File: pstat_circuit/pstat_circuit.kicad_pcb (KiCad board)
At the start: 2 copper layers, 124.5 x 53.3 mm, 40 parts, among them P1 LMP91000-2, P2 LMP91000-2, P3 LMP91000-2, P4 LMP91000-2, P5 LMP91000-2, P6 PWR_BUS, P7 PSTAT_CTRL, P8 I2C_BUS, U1 MCP1700-2, U2 CD4051BM96-2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

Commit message: Replace 10K ohm load resistor with 0.1uF capacitor on 2V5 output of MCP1700
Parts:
- removed R6: 10K, Resistors_SMD:R_0805_HandSoldering
- added C16: 0.1uF, Capacitors_SMD:C_0805_HandSoldering, F.Cu at (81.8, 96.0)
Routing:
- net GND: track 131.2 -> 132.2 mm
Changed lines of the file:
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@@
     (links 133)
     (no_connects 1)
-    (area 67.488999 70.282999 193.019 123.773001)
+    (area 67.488999 70.282999 192.099001 123.773001)
     (thickness 1.6)
     (drawings 23)
-    (tracks 777)
+    (tracks 780)
     (zones 0)
     (modules 40)
@@
   )
   (module Resistors_SMD:R_0805_HandSoldering (layer F.Cu)
-    (at 171.958 100.076 90)
-    (descr "Resistor SMD 0805, hand soldering")
-    (tags "resistor 0805")
-    (attr smd)
-    (fp_text reference R6 (at 3.556 0 90) (layer F.SilkS)
-      (effects (font (size 1 1) (thickness 0.15)))
-    )
-    (fp_text value 10K (at 0 0 90) (layer F.Fab)
-      (effects (font (size 1 1) (thickness 0.15)))
-    )
-    (fp_line (start -2.4 -1) (end 2.4 -1) (layer F.CrtYd) (width 0.05))
-    (fp_line (start -2.4 1) (end 2.4 1) (layer F.CrtYd) (width 0.05))
-    (fp_line (start -2.4 -1) (end -2.4 1) (layer F.CrtYd) (width 0.05))
-    (fp_line (start 2.4 -1) (end 2.4 1) (layer F.CrtYd) (width 0.05))
-    (fp_line (start 0.6 0.875) (end -0.6 0.875) (layer F.SilkS) (width 0.15))
-    (fp_line (start -0.6 -0.875) (end 0.6 -0.875) (layer F.SilkS) (width 0.15))
-    (pad 1 smd rect (at -1.35 0 90) (size 1.5 1.3) (layers F.Cu F.Paste F.Mask)
-      (net 2 GND))
-    (pad 2 smd rect (at 1.35 0 90) (size 1.5 1.3) (layers F.Cu F.Paste F.Mask)
-      (net 3 +2V5))
-    (model Resistors_SMD.3dshapes/R_0805_HandSoldering.wrl
-      (at (xyz 0 0 0))
-      (scale (xyz 1 1 1))
-      (rotate (xyz 0 0 0))
-    )
-  )
-  (module Resistors_SMD:R_0805_HandSoldering (layer F.Cu)
     (at 178.562 95.758 90)
     (descr "Resistor SMD 0805, hand soldering")
@@
       (effects (font (size 1 1) (thickness 0.15)))
     )
-    (fp_text value MCP1700-2 (at -2.286 0 180) (layer F.Fab)
+    (fp_text value MCP1700-2 (at -0.254 0 270) (layer F.Fab)
       (effects (font (size 1 1) (thickness 0.15)))
     )
@@
     (pad 6 smd rect (at -0.95 -1.2 90) (size 0.6 1) (layers F.Cu F.Paste F.Mask)
       (net 2 GND))
+  )
+  (module Capacitors_SMD:C_0805_HandSoldering (layer F.Cu)
+    (at 81.788 96.012 90)
+    (descr "Capacitor SMD 0805, hand soldering")
+    (tags "capacitor 0805")
+    (attr smd)
+    (fp_text reference C16 (at 0 1.778 90) (layer F.SilkS)
+      (effects (font (size 1 1) (thickness 0.15)))
+    )
+    (fp_text value 0.1uF (at 0 0 90) (layer F.Fab)
+      (effects (font (size 1 1) (thickness 0.15)))
+    )
+    (fp_line (start -2.3 -1) (end 2.3 -1) (layer F.CrtYd) (width 0.05))
+    (fp_line (start -2.3 1) (end 2.3 1) (layer F.CrtYd) (width 0.05))
+    (fp_line (start -2.3 -1) (end -2.3 1) (layer F.CrtYd) (width 0.05))
+    (fp_line (start 2.3 -1) (end 2.3 1) (layer F.CrtYd) (width 0.05))
+    (fp_line (start 0.5 -0.85) (end -0.5 -0.85) (layer F.SilkS) (width 0.15))
+    (fp_line (start -0.5 0.85) (end 0.5 0.85) (layer F.SilkS) (width 0.15))
+    (pad 1 smd rect (at -1.25 0 90) (size 1.5 1.25) (layers F.Cu F.Paste F.Mask)
+      (net 3 +2V5))
+    (pad 2 smd rect (at 1.25 0 90) (size 1.5 1.25) (layers F.Cu F.Paste F.Mask)
+      (net 2 GND))
+    (model Capacitors_SMD.3dshapes/C_0805_HandSoldering.wrl
+      (at (xyz 0 0 0))
+      (scale (xyz 1 1 1))
+      (rotate (xyz 0 0 0))
+    )
   )
   (gr_text SDA (at 186.944 77.216 90) (layer F.Cu)
@@
   (segment (start 180.34 121.412) (end 184.658 117.094) (width 0.25) (layer B.Cu) (net 1))
   (segment (start 186.088 88.773) (end 186.563 88.773) (width 0.25) (layer F.Cu) (net 1))
+  (segment (start 172.994 106.172) (end 171.978 105.156) (width 0.25) (layer F.Cu) (net 2))
+  (via (at 171.958 104.14) (size 1.5) (drill 0.6) (layers F.Cu B.Cu) (net 2))
+  (segment (start 171.978 104.16) (end 171.958 104.14) (width 0.25) (layer F.Cu) (net 2))
+  (segment (start 171.978 105.156) (end 171.978 104.16) (width 0.25) (layer F.Cu) (net 2))
+  (segment (start 81.788 94.762) (end 80.752 93.726) (width 0.25) (layer F.Cu) (net 2))
+  (segment (start 80.752 93.726) (end 78.486 93.726) (width 0.25) (layer F.Cu) (net 2))
   (segment (start 163.322 92.202) (end 163.322 94.234) (width 0.25) (layer F.Cu) (net 2))
   (segment (start 162.814 89.916) (end 163.322 90.424) (width 0.25) (layer F.Cu) (net 2))
@@
   (segment (start 128.27 88.9) (end 128.27 89.916) (width 0.25) (layer F.Cu) (net 2))
   (via (at 128.27 89.916) (size 1.5) (drill 0.6) (layers F.Cu B.Cu) (net 2))
-  (segment (start 171.958 101.426) (end 171.958 104.14) (width 0.25) (layer F.Cu) (net 2))
-  (segment (start 171.958 105.136) (end 171.958 104.14) (width 0.25) (layer F.Cu) (net 2))
-  (via (at 171.958 104.14) (size 1.5) (drill 0.6) (layers F.Cu B.Cu) (net 2))
-  (segment (start 171.958 105.136) (end 172.994 106.172) (width 0.25) (layer F.Cu) (net 2))
   (segment (start 133.624 106.172) (end 132.588 105.136) (width 0.25) (layer F.Cu) (net 2))
   (via (at 132.588 104.14) (size 1.5) (drill 0.6) (layers F.Cu B.Cu) (net 2))
@@
   (segment (start 169.672 93.472) (end 169.672 92.71) (width 0.25) (layer F.Cu) (net 2))
   (segment (start 169.672 92.71) (end 169.672 92.202) (width 0.25) (layer F.Cu) (net 2))
+  (segment (start 81.788 97.008) (end 82.316 97.536) (width 0.25) (layer F.Cu) (net 3))
+  (segment (start 82.316 97.536) (end 83.312 97.536) (width 0.25) (layer F.Cu) (net 3))
+  (segment (start 79.636 96.332) (end 81.112 96.332) (width 0.25) (layer F.Cu) (net 3))
+  (segment (start 81.112 96.332) (end 81.788 97.008) (width 0.25) (layer F.Cu) (net 3))
   (segment (start 85.344 94.996) (end 85.344 87.904) (width 0.25) (layer F.Cu) (net 3))
   (segment (start 85.344 87.904) (end 85.364 87.884) (width 0.25) (layer F.Cu) (net 3))
@@
   (segment (start 175.494 99.294) (end 174.752 98.552) (width 0.25) (layer F.Cu) (net 3))
   (segment (start 174.752 98.552) (end 171.958 98.552) (width 0.25) (layer F.Cu) (net 3))
-  (segment (start 81.28 97.536) (end 81.788 97.536) (width 0.25) (layer F.Cu) (net 3))
-  (segment (start 85.344 97.536) (end 81.788 97.536) (width 0.25) (layer F.Cu) (net 3))
-  (segment (start 81.28 97.536) (end 80.076 96.332) (width 0.25) (layer F.Cu) (net 3))
+  (segment (start 85.344 97.536) (end 83.312 97.536) (width 0.25) (layer F.Cu) (net 3))
   (segment (start 175.494 106.172) (end 175.494 99.294) (width 0.25) (layer F.Cu) (net 3))
   (segment (start 178.064 106.958) (end 176.28 106.958) (width 0.25) (layer F.Cu) (net 3))
@@
   (segment (start 136.144 99.822) (end 136.144 106.152) (width 0.25) (layer F.Cu) (net 3))
   (segment (start 136.144 106.152) (end 136.124 106.172) (width 0.25) (layer F.Cu) (net 3))
-  (segment (start 80.076 96.332) (end 79.636 96.332) (width 0.25) (layer F.Cu) (net 3))
   (segment (start 136.144 98.552) (end 134.62 98.552) (width 0.25) (layer F.Cu) (net 3))
   (segment (start 134.112 98.044) (end 132.588 98.044) (width 0.25) (layer F.Cu) (net 3))

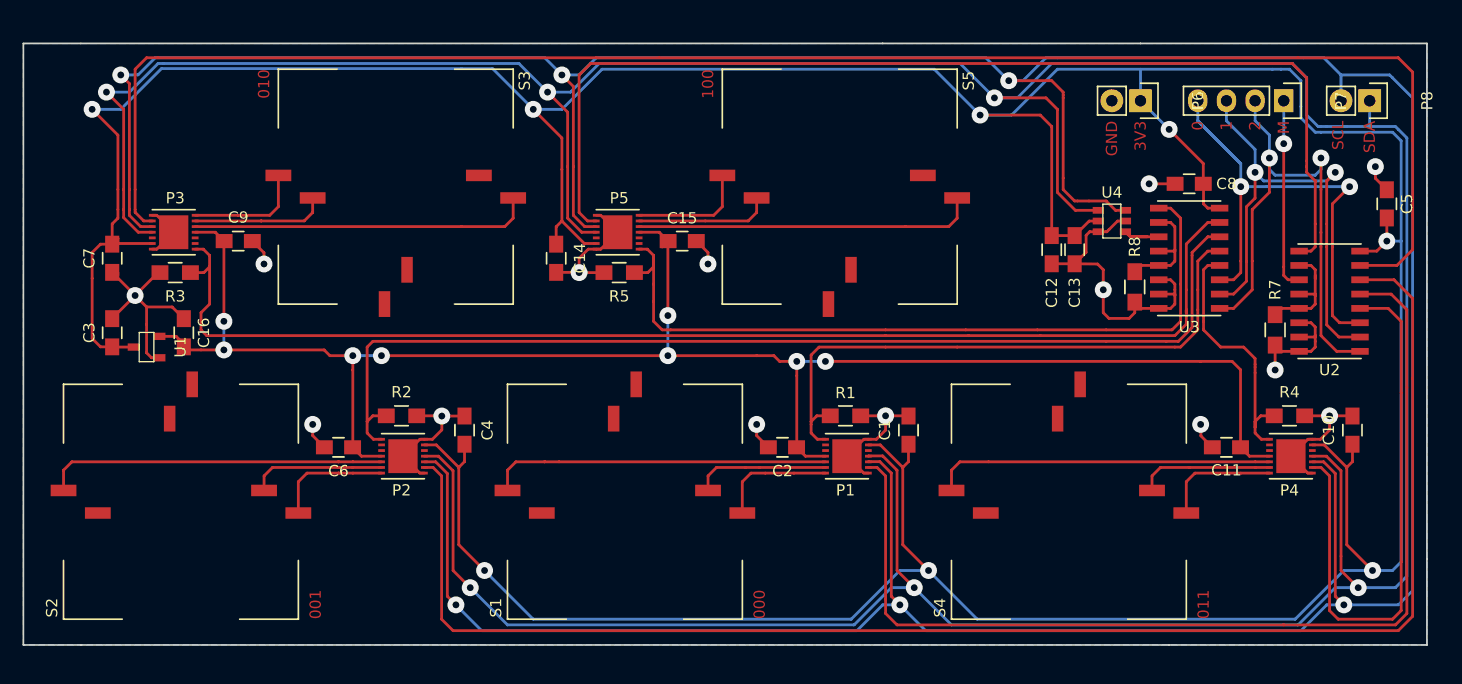
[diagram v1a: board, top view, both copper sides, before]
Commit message: Widen traces on pstat breakout
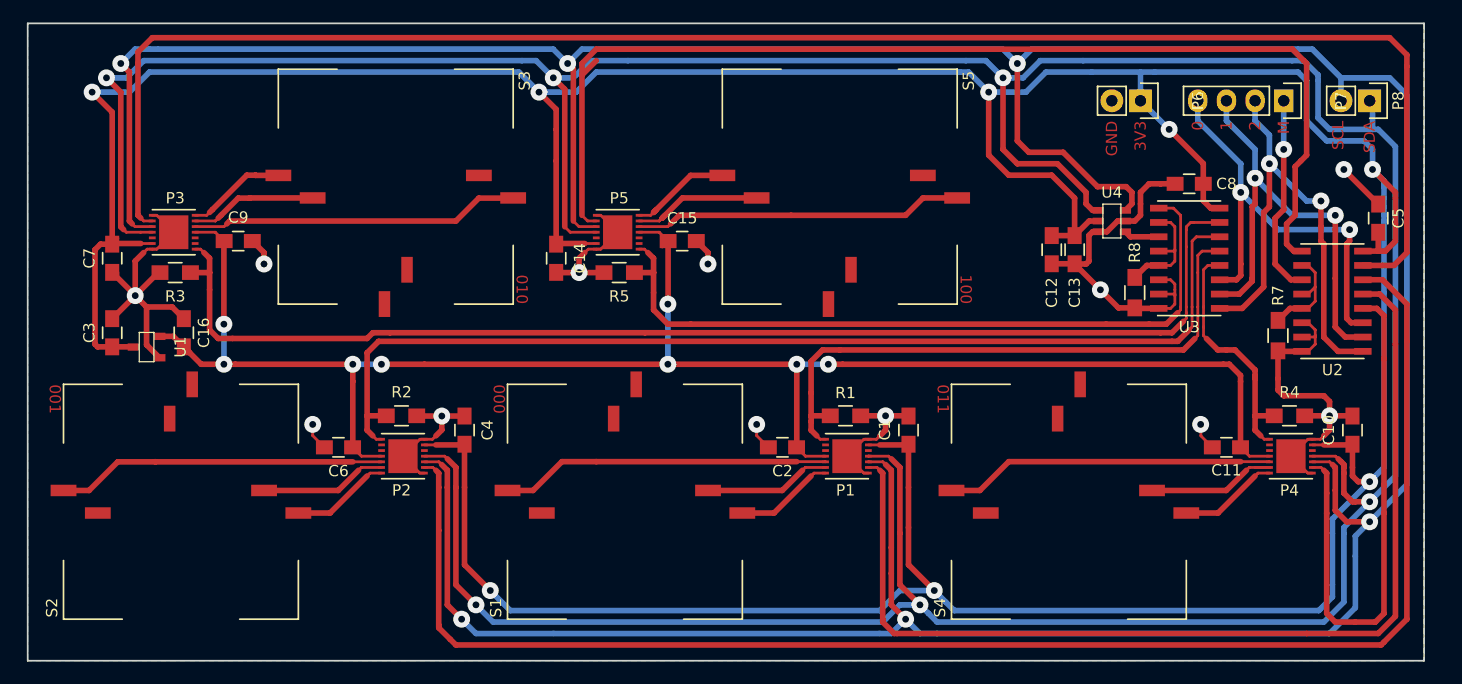
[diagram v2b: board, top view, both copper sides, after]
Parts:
- moved C5 1.48 mm to (187.7, 85.9)
- moved R7 0.57 mm to (178.8, 96.3)
- moved R8 0.51 mm to (166.1, 92.5)
- moved U2 0.25 mm to (183.6, 93.2)
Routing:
- net GND: track 132.2 -> 146.2 mm, vias 14 -> 12
- net +3V3: track 394.3 -> 385.2 mm
- net /PSEL0: track 48.8 -> 39.7 mm
- net /SDA: track 345.7 -> 339.1 mm
- net Net-(P5-Pad2): track 96.5 -> 102.2 mm
- net /PSEL1: track 46.3 -> 41.7 mm
- net /PSEL2: track 48.3 -> 44.0 mm
- net /SCL: track 349.2 -> 345.4 mm
- net Net-(P5-Pad8): track 69.1 -> 66.3 mm
- net Net-(P4-Pad2): track 50.5 -> 48.2 mm
- net +2V5: track 154.8 -> 157.0 mm
- net /VSTAT: track 5.27 -> 3.14 mm
- net Net-(P3-Pad2): track 149.8 -> 151.5 mm
- net Net-(P2-Pad14): track 10.5 -> 8.85 mm
- net Net-(P4-Pad14): track 10.5 -> 8.85 mm
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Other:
- board size 124.5 x 53.3 mm -> 123.8 x 56.5 mm
- rule trace_min: 0.2 -> 0.25
- rule via_min_drill: 0.3 -> 0.6
- rule via_min_size: 0.4 -> 1.5

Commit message: Remove deadend trace
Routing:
- net Net-(P5-Pad2): track 102.2 -> 98.6 mm
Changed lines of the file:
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@@
     (links 133)
     (no_connects 0)
-    (area 67.488999 70.282999 193.019 123.773001)
+    (area 67.869999 68.504999 191.845001 125.170001)
     (thickness 1.6)
     (drawings 18)
-    (tracks 852)
+    (tracks 850)
     (zones 0)
     (modules 40)
@@
   (layers
     (0 F.Cu signal)
-    (31 B.Cu signal)
+    (31 B.Cu signal hide)
     (32 B.Adhes user)
     (33 F.Adhes user)
@@
   (segment (start 117.594 86.098) (end 117.094 85.598) (width 0.25) (layer F.Cu) (net 26))
   (segment (start 117.594 86.098) (end 118.364 86.098) (width 0.25) (layer F.Cu) (net 26))
-  (segment (start 117.094 73.152) (end 118.364 71.882) (width 0.5) (layer F.Cu) (net 26))
-  (segment (start 117.094 73.152) (end 118.364 71.882) (width 0.25) (layer F.Cu) (net 26))
   (segment (start 179.578 88.138) (end 180.213 88.773) (width 0.5) (layer F.Cu) (net 26))
   (segment (start 179.578 88.138) (end 179.578 86.36) (width 0.5) (layer F.Cu) (net 26))
